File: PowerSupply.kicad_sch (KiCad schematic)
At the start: 42 parts, among them Q201 BSS138, Q202 SQJA62EP-T1_GE3, U201 LM3478MM, U202 MCP1703A-3302

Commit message: add git hash
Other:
- title: (none) -> ZM108x, Z57x nixieboard
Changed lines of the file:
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@@
 (kicad_sch (version 20230121) (generator eeschema)
   (paper "A4")
+  (title_block
+    (title "ZM108x, Z57x nixieboard")
+    (date "2025-09-04")
+    (rev "3/${GITHASH}")
+    (comment 1 "Atuthor: Martin Sabol")
+  )
   (junction (at 182.88 72.39) (diameter 0) (color 0 0 0 0)
   )

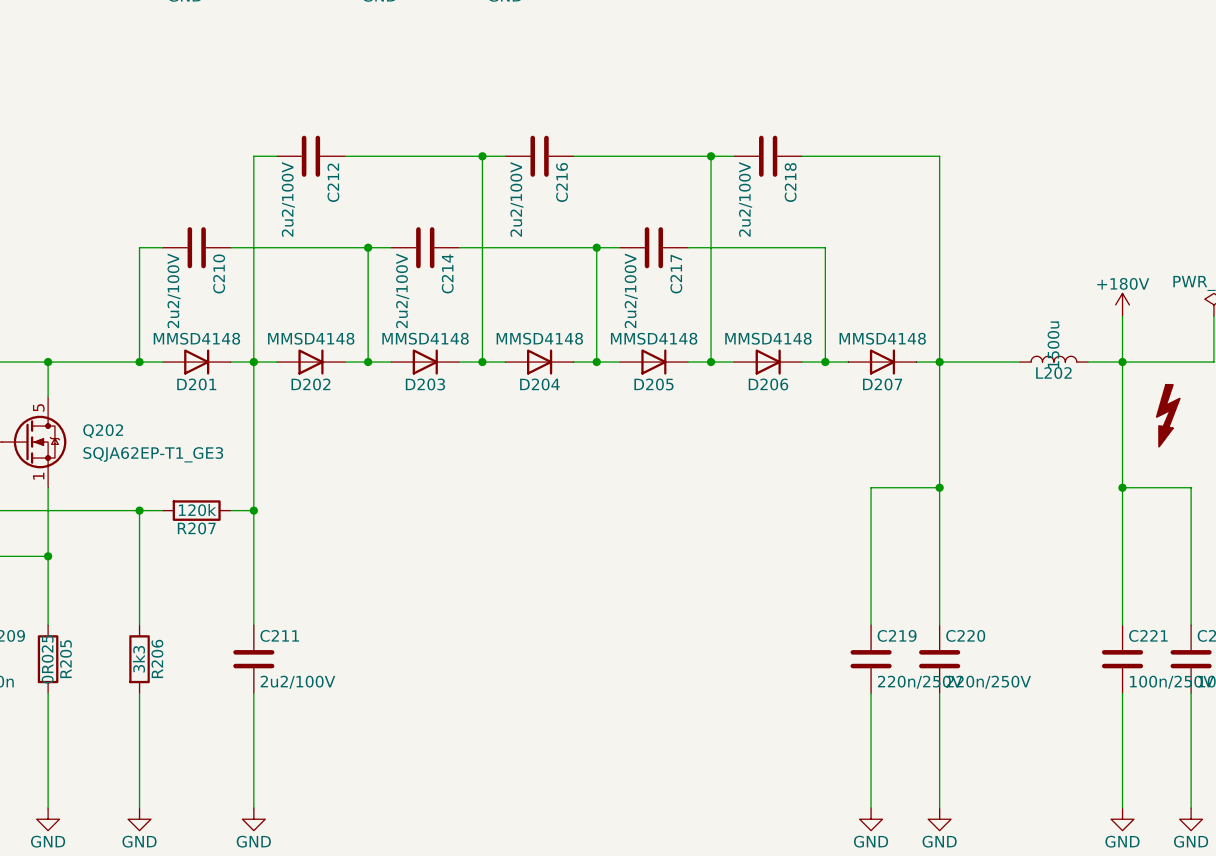
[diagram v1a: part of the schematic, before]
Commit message: schema: bom: PNs update
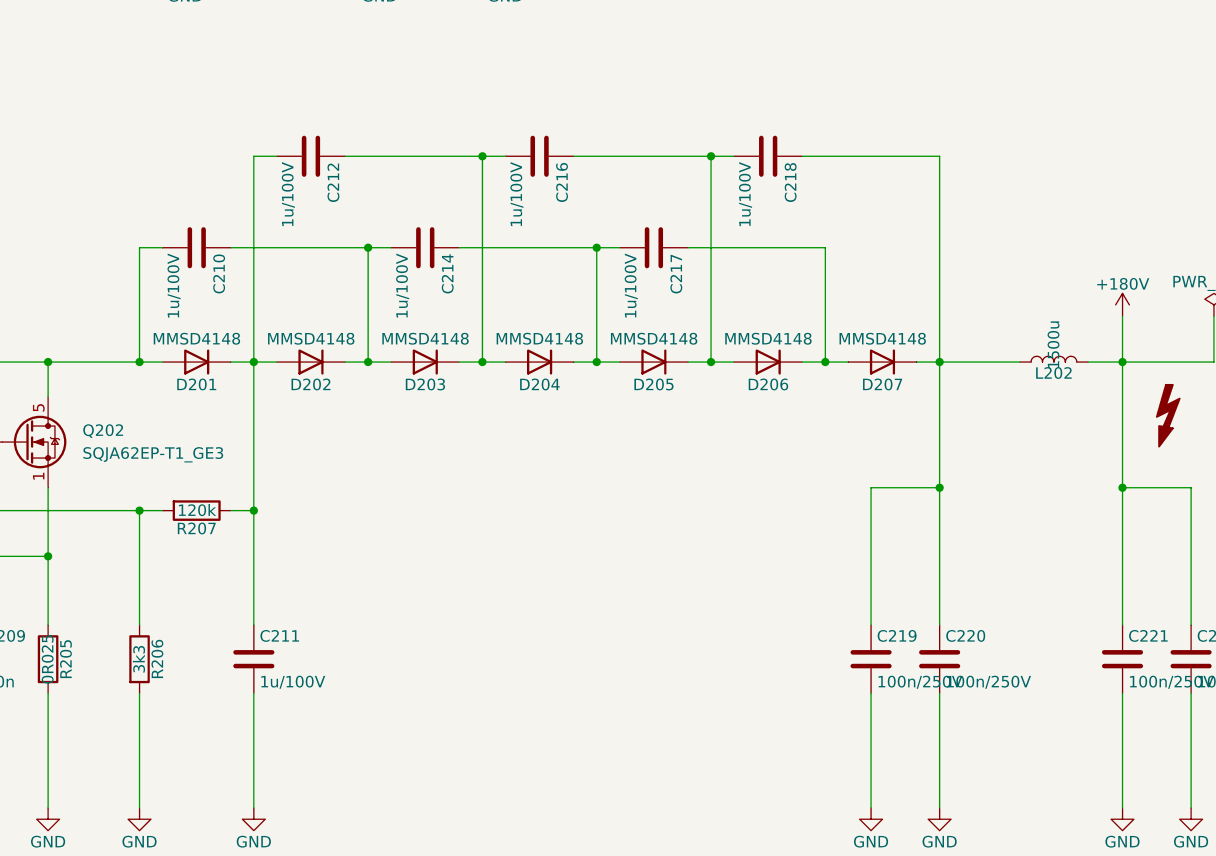
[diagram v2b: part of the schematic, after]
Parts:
- C201, C202, C203, C204, C207: SPN CL32A107MQVNNNE -> CL31A476MQHNNNE
- C205: SPN CL10B105KO8NNNC -> CL21B105KOFNNNE
- C206: SPN CL10B105KO8NNNC -> CC0805KRX7R9BB223
- C208, C213, C215: SPN CL32A107MQVNNNE -> CL21B103KBANNNC
- C210, C211, C212, C214, C216, C217, C218: value 2u2/100V -> 1u/100V; SPN CL32B225KCJSNNE -> CL31B105KCHSNNE
- C219, C220: value 220n/250V -> 100n/250V; SPN GRM32DR72E224KW01L -> GRM31CR72E104KW03L
- C221, C222: SPN GRM32DR72E104KW01L -> GRM31CR72E104KW03L
- Q201: SPN (none) -> BSS138
- Q202: SPN (none) -> PSMN013-60YLX
- R201, R202: SPN SMD0603-470K-1% -> 0805S8F1002T5E
- R203: SPN SMD0603-470K-1% -> 0805S8F1803T5E
- R204: SPN SMD0603-470K-1% -> 0805S8F4701T5E
- R205: SPN CS0603-0R033-5% -> CS05FTJWR033
- R206: SPN RC0603FR-073K3 -> 0805S8F3301T5E
- R207: SPN RC0805JR-07120K -> 0805S8F1203T5E
- U201: SPN (none) -> LM3478MMX/NOPB
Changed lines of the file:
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@@
       (effects (font (size 1.27 1.27)) hide)
     )
-    (property "SPN" "CL32A107MQVNNNE" (at 171.45 44.45 0)
+    (property "SPN" "CL21B103KBANNNC" (at 171.45 44.45 0)
       (effects (font (size 1.27 1.27)) hide)
     )
@@
       (effects (font (size 1.27 1.27)) hide)
     )
-    (property "SPN" "RC0805JR-07120K" (at 151.13 111.76 0)
+    (property "SPN" "0805S8F1203T5E" (at 151.13 111.76 0)
       (effects (font (size 1.27 1.27)) hide)
     )
@@
       (effects (font (size 1.27 1.27)) hide)
     )
-    (property "SPN" "RC0603FR-073K3" (at 144.78 128.27 0)
+    (property "SPN" "0805S8F3301T5E" (at 144.78 128.27 0)
       (effects (font (size 1.27 1.27)) hide)
     )
@@
       (effects (font (size 1.27 1.27)) (justify left))
     )
-    (property "Value" "2u2/100V" (at 158.115 130.81 0)
+    (property "Value" "1u/100V" (at 158.115 130.81 0)
       (effects (font (size 1.27 1.27)) (justify left))
     )
@@
       (effects (font (size 1.27 1.27)) hide)
     )
-    (property "SPN" "CL32B225KCJSNNE" (at 157.48 128.27 0)
+    (property "SPN" "CL31B105KCHSNNE" (at 157.48 128.27 0)
       (effects (font (size 1.27 1.27)) hide)
     )
@@
       (effects (font (size 1.27 1.27)) (justify left))
     )
-    (property "Value" "2u2/100V" (at 148.59 83.185 0)
+    (property "Value" "1u/100V" (at 148.59 83.185 0)
       (effects (font (size 1.27 1.27)) (justify left))
     )
@@
       (effects (font (size 1.27 1.27)) hide)
     )
-    (property "SPN" "CL32B225KCJSNNE" (at 151.13 82.55 0)
+    (property "SPN" "CL31B105KCHSNNE" (at 151.13 82.55 0)
       (effects (font (size 1.27 1.27)) hide)
     )
@@
       (effects (font (size 1.27 1.27)) (justify left))
     )
-    (property "Value" "2u2/100V" (at 161.29 73.025 0)
+    (property "Value" "1u/100V" (at 161.29 73.025 0)
       (effects (font (size 1.27 1.27)) (justify left))
     )
@@
       (effects (font (size 1.27 1.27)) hide)
     )
-    (property "SPN" "CL32B225KCJSNNE" (at 163.83 72.39 0)
+    (property "SPN" "CL31B105KCHSNNE" (at 163.83 72.39 0)
       (effects (font (size 1.27 1.27)) hide)
     )
@@
       (effects (font (size 1.27 1.27)) (justify left))
     )
-    (property "Value" "2u2/100V" (at 173.99 83.185 0)
+    (property "Value" "1u/100V" (at 173.99 83.185 0)
       (effects (font (size 1.27 1.27)) (justify left))
     )
@@
       (effects (font (size 1.27 1.27)) hide)
     )
-    (property "SPN" "CL32B225KCJSNNE" (at 176.53 82.55 0)
+    (property "SPN" "CL31B105KCHSNNE" (at 176.53 82.55 0)
       (effects (font (size 1.27 1.27)) hide)
     )
@@
       (effects (font (size 1.27 1.27)) (justify left))
     )
-    (property "Value" "2u2/100V" (at 186.69 73.025 0)
+    (property "Value" "1u/100V" (at 186.69 73.025 0)
       (effects (font (size 1.27 1.27)) (justify left))
     )
@@
       (effects (font (size 1.27 1.27)) hide)
     )
-    (property "SPN" "CL32B225KCJSNNE" (at 189.23 72.39 0)
+    (property "SPN" "CL31B105KCHSNNE" (at 189.23 72.39 0)
       (effects (font (size 1.27 1.27)) hide)
     )
@@
       (effects (font (size 1.27 1.27)) (justify left))
     )
-    (property "Value" "2u2/100V" (at 199.39 83.185 0)
+    (property "Value" "1u/100V" (at 199.39 83.185 0)
       (effects (font (size 1.27 1.27)) (justify left))
     )
@@
       (effects (font (size 1.27 1.27)) hide)
     )
-    (property "SPN" "CL32B225KCJSNNE" (at 201.93 82.55 0)
+    (property "SPN" "CL31B105KCHSNNE" (at 201.93 82.55 0)
       (effects (font (size 1.27 1.27)) hide)
     )
@@
       (effects (font (size 1.27 1.27)) (justify left))
     )
-    (property "Value" "2u2/100V" (at 212.09 73.025 0)
+    (property "Value" "1u/100V" (at 212.09 73.025 0)
       (effects (font (size 1.27 1.27)) (justify left))
     )
@@
       (effects (font (size 1.27 1.27)) hide)
     )
-    (property "SPN" "CL32B225KCJSNNE" (at 214.63 72.39 0)
+    (property "SPN" "CL31B105KCHSNNE" (at 214.63 72.39 0)
       (effects (font (size 1.27 1.27)) hide)
     )
@@
       (effects (font (size 1.27 1.27)) (justify left))
     )
-    (property "Value" "220n/250V" (at 226.695 130.81 0)
+    (property "Value" "100n/250V" (at 226.695 130.81 0)
       (effects (font (size 1.27 1.27)) (justify left))
     )
@@
       (effects (font (size 1.27 1.27)) hide)
     )
-    (property "SPN" "GRM32DR72E224KW01L" (at 226.06 128.27 0)
+    (property "SPN" "GRM31CR72E104KW03L" (at 226.06 128.27 0)
       (effects (font (size 1.27 1.27)) hide)
     )
@@
       (effects (font (size 1.27 1.27)) (justify left))
     )
-    (property "Value" "220n/250V" (at 234.315 130.81 0)
+    (property "Value" "100n/250V" (at 234.315 130.81 0)
       (effects (font (size 1.27 1.27)) (justify left))
     )
@@
       (effects (font (size 1.27 1.27)) hide)
     )
-    (property "SPN" "GRM32DR72E224KW01L" (at 233.68 128.27 0)
+    (property "SPN" "GRM31CR72E104KW03L" (at 233.68 128.27 0)
       (effects (font (size 1.27 1.27)) hide)
     )
@@
       (effects (font (size 1.27 1.27)) hide)
     )
-    (property "SPN" "CS0603-0R033-5%" (at 134.62 128.27 0)
+    (property "SPN" "CS05FTJWR033" (at 134.62 128.27 0)
       (effects (font (size 1.27 1.27)) hide)
     )
@@
       (effects (font (size 1.27 1.27)) hide)
     )
-    (property "SPN" "GRM32DR72E104KW01L" (at 261.62 128.27 0)
+    (property "SPN" "GRM31CR72E104KW03L" (at 261.62 128.27 0)
       (effects (font (size 1.27 1.27)) hide)
     )
@@
       (effects (font (size 1.27 1.27)) hide)
     )
-    (property "SPN" "GRM32DR72E104KW01L" (at 254 128.27 0)
+    (property "SPN" "GRM31CR72E104KW03L" (at 254 128.27 0)
       (effects (font (size 1.27 1.27)) hide)
     )
@@
       (effects (font (size 1.27 1.27)) hide)
     )
-    (property "SPN" "CL10B105KO8NNNC" (at 73.66 105.41 0)
+    (property "SPN" "CL21B105KOFNNNE" (at 73.66 105.41 0)
       (effects (font (size 1.27 1.27)) hide)
     )
@@
       (effects (font (size 1.27 1.27)) hide)
     )
-    (property "SPN" "CL32A107MQVNNNE" (at 36.83 105.41 0)
+    (property "SPN" "CL31A476MQHNNNE" (at 36.83 105.41 0)
       (effects (font (size 1.27 1.27)) hide)
     )
@@
       (effects (font (size 1.27 1.27)) hide)
     )
-    (property "SPN" "CL32A107MQVNNNE" (at 49.53 105.41 0)
+    (property "SPN" "CL31A476MQHNNNE" (at 49.53 105.41 0)
       (effects (font (size 1.27 1.27)) hide)
     )
@@
       (effects (font (size 1.27 1.27)) hide)
     )
-    (property "SPN" "CL32A107MQVNNNE" (at 24.13 105.41 0)
+    (property "SPN" "CL31A476MQHNNNE" (at 24.13 105.41 0)
       (effects (font (size 1.27 1.27)) hide)
     )
@@
       (effects (font (size 1.27 1.27)) hide)
     )
-    (property "SPN" "CL32A107MQVNNNE" (at 185.42 44.45 0)
+    (property "SPN" "CL21B103KBANNNC" (at 185.42 44.45 0)
       (effects (font (size 1.27 1.27)) hide)
     )
@@
       (effects (font (size 1.27 1.27)) hide)
     )
-    (property "SPN" "CL32A107MQVNNNE" (at 125.73 44.45 0)
+    (property "SPN" "CL21B103KBANNNC" (at 125.73 44.45 0)
       (effects (font (size 1.27 1.27)) hide)
     )
@@
       (effects (font (size 1.27 1.27)) hide)
     )
-    (property "SPN" "CL32A107MQVNNNE" (at 113.03 44.45 0)
+    (property "SPN" "CL31A476MQHNNNE" (at 113.03 44.45 0)
       (effects (font (size 1.27 1.27)) hide)
     )
@@
       (effects (font (size 1.27 1.27)) hide)
     )
-    (property "SPN" "CL32A107MQVNNNE" (at 60.96 105.41 0)
+    (property "SPN" "CL31A476MQHNNNE" (at 60.96 105.41 0)
       (effects (font (size 1.27 1.27)) hide)
     )
@@
       (effects (font (size 1.27 1.27)) hide)
     )
-    (property "SPN" "SMD0603-470K-1%" (at 95.25 134.62 0)
+    (property "SPN" "0805S8F4701T5E" (at 95.25 134.62 0)
       (effects (font (size 1.27 1.27)) hide)
     )
@@
     )
     (property "Datasheet" "https://www.ti.com/lit/gpn/lm3478" (at 112.395 99.06 0)
+      (effects (font (size 1.27 1.27)) hide)
+    )
+    (property "SPN" "LM3478MMX/NOPB" (at 111.76 111.76 0)
       (effects (font (size 1.27 1.27)) hide)
     )
@@
       (effects (font (size 1.27 1.27)) hide)
     )
-    (property "SPN" "SMD0603-470K-1%" (at 85.09 119.38 0)
+    (property "SPN" "0805S8F1803T5E" (at 85.09 119.38 0)
       (effects (font (size 1.27 1.27)) hide)
     )
@@
       (effects (font (size 1.27 1.27)) hide)
     )
-    (property "SPN" "SMD0603-470K-1%" (at 85.09 105.41 0)
+    (property "SPN" "0805S8F1002T5E" (at 85.09 105.41 0)
       (effects (font (size 1.27 1.27)) hide)
     )
@@
       (effects (font (size 1.27 1.27)) hide)
     )
-    (property "SPN" "CL10B105KO8NNNC" (at 95.25 123.19 0)
+    (property "SPN" "CC0805KRX7R9BB223" (at 95.25 123.19 0)
       (effects (font (size 1.27 1.27)) hide)
     )
@@
       (effects (font (size 1.27 1.27)) hide)
     )
-    (property "SPN" "SMD0603-470K-1%" (at 72.39 138.43 0)
+    (property "SPN" "0805S8F1002T5E" (at 72.39 138.43 0)
       (effects (font (size 1.27 1.27)) hide)
     )
@@
       (effects (font (size 1.27 1.27)) (justify left) hide)
     )
+    (property "SPN" "BSS138" (at 82.55 132.08 0)
+      (effects (font (size 1.27 1.27)) hide)
+    )
     (pin "1")
     (pin "2")
@@
       (effects (font (size 1.27 1.27)) (justify left) hide)
     )
+    (property "SPN" "PSMN013-60YLX" (at 132.08 104.14 0)
+      (effects (font (size 1.27 1.27)) hide)
+    )
     (pin "5")
